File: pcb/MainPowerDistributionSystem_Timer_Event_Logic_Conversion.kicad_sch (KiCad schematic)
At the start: 4 parts

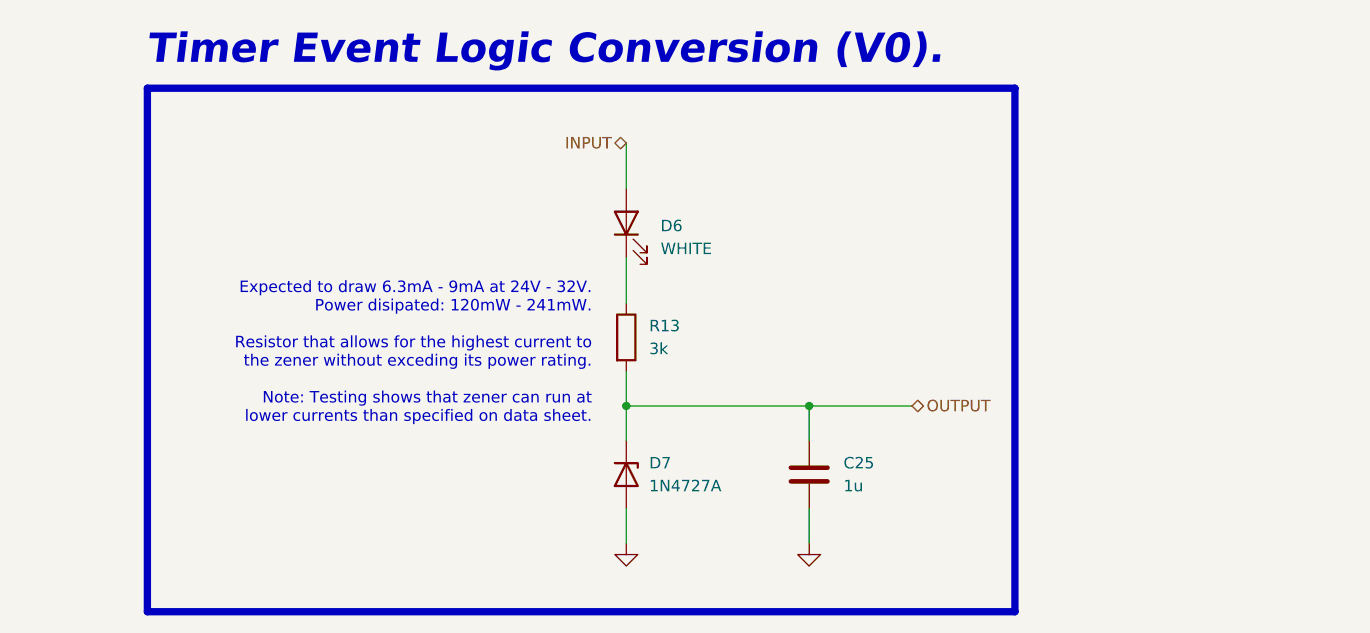
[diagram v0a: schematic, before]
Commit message: Fixed issues reported by `checkPCBs` concerning the stack connectors.
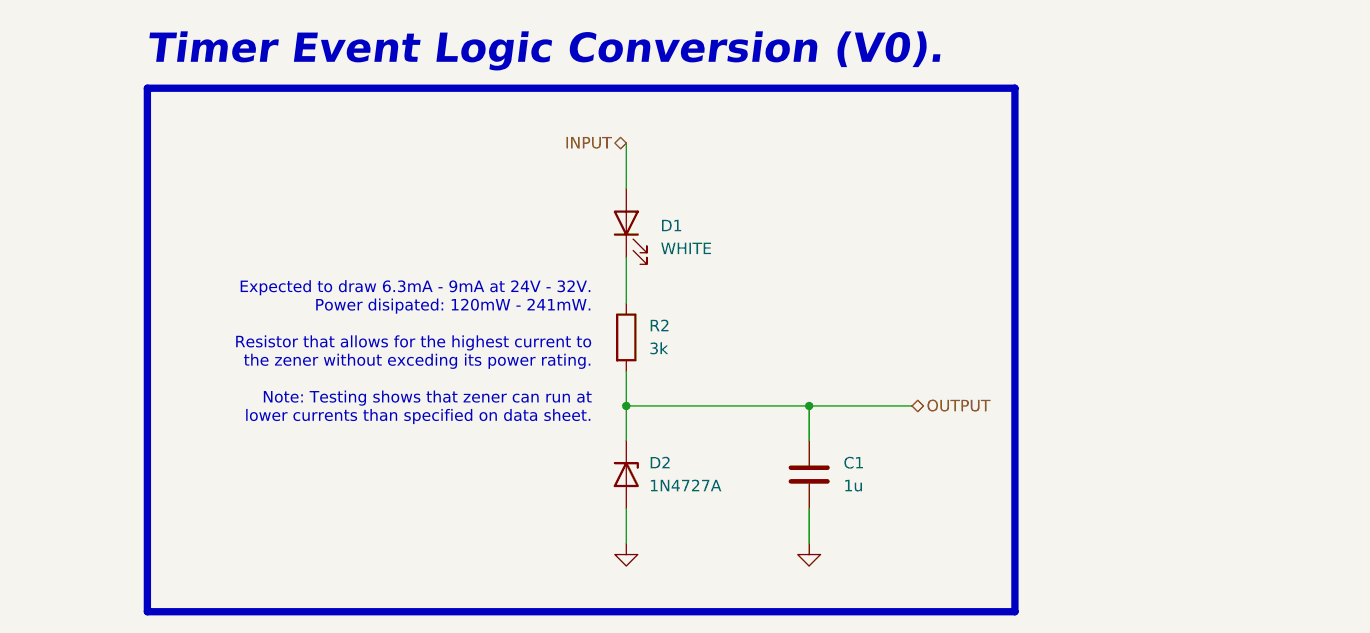
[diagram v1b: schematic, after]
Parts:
- renumbered C25 to C1, D6 to D1, D7 to D2, R13 to R2
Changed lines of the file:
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@@
 		(dnp no)
 		(fields_autoplaced yes)
-		(property "Reference" "C25"
+		(property "Reference" "C1"
 			(at 138.43 91.4399 0)
 			(effects
@@
 				(path "/92a7a41c-8494-4e4b-ac2d-deb1f1cd8085/54620fe3-2093-4758-a776-838cd07d45c6"
 					(reference "C25")
+					(unit 1)
+				)
+			)
+			(project "MainPowerDistributionSystem"
+				(path "/f4672588-55b2-48e9-8f23-132a69134eb2/261c9762-dbc6-4b8c-91f7-76f368e53a64"
+					(reference "C1")
+					(unit 1)
+				)
+				(path "/f4672588-55b2-48e9-8f23-132a69134eb2/3f92f74e-3cca-4282-aab2-357fe1c1118f"
+					(reference "C3")
+					(unit 1)
+				)
+				(path "/f4672588-55b2-48e9-8f23-132a69134eb2/41b9944a-f63d-4ce0-843f-6c1f8b109fe2"
+					(reference "C20")
+					(unit 1)
+				)
+				(path "/f4672588-55b2-48e9-8f23-132a69134eb2/5794667a-7b17-4495-a615-6983a1fee026"
+					(reference "C2")
+					(unit 1)
+				)
+				(path "/f4672588-55b2-48e9-8f23-132a69134eb2/5cd708ab-f243-4c3d-b9a6-6ef81c5046b4"
+					(reference "C21")
+					(unit 1)
+				)
+				(path "/f4672588-55b2-48e9-8f23-132a69134eb2/7bfeb19b-cfbf-4688-9fe2-f6b9e19ab4b8"
+					(reference "C19")
+					(unit 1)
+				)
+				(path "/f4672588-55b2-48e9-8f23-132a69134eb2/808cc913-2635-4e01-9a87-a42fd91b330a"
+					(reference "C18")
 					(unit 1)
 				)
@@
 		(dnp no)
 		(fields_autoplaced yes)
-		(property "Reference" "#PWR014"
+		(property "Reference" "#PWR056"
 			(at 114.3 106.68 0)
 			(effects
@@
 				(path "/92a7a41c-8494-4e4b-ac2d-deb1f1cd8085/54620fe3-2093-4758-a776-838cd07d45c6"
 					(reference "#PWR014")
+					(unit 1)
+				)
+			)
+			(project "MainPowerDistributionSystem"
+				(path "/f4672588-55b2-48e9-8f23-132a69134eb2/261c9762-dbc6-4b8c-91f7-76f368e53a64"
+					(reference "#PWR056")
+					(unit 1)
+				)
+				(path "/f4672588-55b2-48e9-8f23-132a69134eb2/3f92f74e-3cca-4282-aab2-357fe1c1118f"
+					(reference "#PWR060")
+					(unit 1)
+				)
+				(path "/f4672588-55b2-48e9-8f23-132a69134eb2/41b9944a-f63d-4ce0-843f-6c1f8b109fe2"
+					(reference "#PWR078")
+					(unit 1)
+				)
+				(path "/f4672588-55b2-48e9-8f23-132a69134eb2/5794667a-7b17-4495-a615-6983a1fee026"
+					(reference "#PWR058")
+					(unit 1)
+				)
+				(path "/f4672588-55b2-48e9-8f23-132a69134eb2/5cd708ab-f243-4c3d-b9a6-6ef81c5046b4"
+					(reference "#PWR080")
+					(unit 1)
+				)
+				(path "/f4672588-55b2-48e9-8f23-132a69134eb2/7bfeb19b-cfbf-4688-9fe2-f6b9e19ab4b8"
+					(reference "#PWR076")
+					(unit 1)
+				)
+				(path "/f4672588-55b2-48e9-8f23-132a69134eb2/808cc913-2635-4e01-9a87-a42fd91b330a"
+					(reference "#PWR074")
 					(unit 1)
 				)
@@
 		(dnp no)
 		(fields_autoplaced yes)
-		(property "Reference" "D6"
+		(property "Reference" "D1"
 			(at 118.11 65.0874 90)
 			(effects
@@
 				(path "/92a7a41c-8494-4e4b-ac2d-deb1f1cd8085/54620fe3-2093-4758-a776-838cd07d45c6"
 					(reference "D6")
+					(unit 1)
+				)
+			)
+			(project "MainPowerDistributionSystem"
+				(path "/f4672588-55b2-48e9-8f23-132a69134eb2/261c9762-dbc6-4b8c-91f7-76f368e53a64"
+					(reference "D1")
+					(unit 1)
+				)
+				(path "/f4672588-55b2-48e9-8f23-132a69134eb2/3f92f74e-3cca-4282-aab2-357fe1c1118f"
+					(reference "D5")
+					(unit 1)
+				)
+				(path "/f4672588-55b2-48e9-8f23-132a69134eb2/41b9944a-f63d-4ce0-843f-6c1f8b109fe2"
+					(reference "D11")
+					(unit 1)
+				)
+				(path "/f4672588-55b2-48e9-8f23-132a69134eb2/5794667a-7b17-4495-a615-6983a1fee026"
+					(reference "D3")
+					(unit 1)
+				)
+				(path "/f4672588-55b2-48e9-8f23-132a69134eb2/5cd708ab-f243-4c3d-b9a6-6ef81c5046b4"
+					(reference "D13")
+					(unit 1)
+				)
+				(path "/f4672588-55b2-48e9-8f23-132a69134eb2/7bfeb19b-cfbf-4688-9fe2-f6b9e19ab4b8"
+					(reference "D9")
+					(unit 1)
+				)
+				(path "/f4672588-55b2-48e9-8f23-132a69134eb2/808cc913-2635-4e01-9a87-a42fd91b330a"
+					(reference "D7")
 					(unit 1)
 				)
@@
 		(dnp no)
 		(fields_autoplaced yes)
-		(property "Reference" "R13"
+		(property "Reference" "R2"
 			(at 116.84 76.1999 0)
 			(effects
@@
 			(project "VehiclePowerDistributionSystem"
 				(path "/92a7a41c-8494-4e4b-ac2d-deb1f1cd8085/54620fe3-2093-4758-a776-838cd07d45c6"
+					(reference "R13")
+					(unit 1)
+				)
+			)
+			(project "MainPowerDistributionSystem"
+				(path "/f4672588-55b2-48e9-8f23-132a69134eb2/261c9762-dbc6-4b8c-91f7-76f368e53a64"
+					(reference "R2")
+					(unit 1)
+				)
+				(path "/f4672588-55b2-48e9-8f23-132a69134eb2/3f92f74e-3cca-4282-aab2-357fe1c1118f"
+					(reference "R4")
+					(unit 1)
+				)
+				(path "/f4672588-55b2-48e9-8f23-132a69134eb2/41b9944a-f63d-4ce0-843f-6c1f8b109fe2"
+					(reference "R15")
+					(unit 1)
+				)
+				(path "/f4672588-55b2-48e9-8f23-132a69134eb2/5794667a-7b17-4495-a615-6983a1fee026"
+					(reference "R3")
+					(unit 1)
+				)
+				(path "/f4672588-55b2-48e9-8f23-132a69134eb2/5cd708ab-f243-4c3d-b9a6-6ef81c5046b4"
+					(reference "R16")
+					(unit 1)
+				)
+				(path "/f4672588-55b2-48e9-8f23-132a69134eb2/7bfeb19b-cfbf-4688-9fe2-f6b9e19ab4b8"
+					(reference "R14")
+					(unit 1)
+				)
+				(path "/f4672588-55b2-48e9-8f23-132a69134eb2/808cc913-2635-4e01-9a87-a42fd91b330a"
 					(reference "R13")
 					(unit 1)
@@
 		(dnp no)
 		(fields_autoplaced yes)
-		(property "Reference" "#PWR015"
+		(property "Reference" "#PWR057"
 			(at 134.62 106.68 0)
 			(effects
@@
 				(path "/92a7a41c-8494-4e4b-ac2d-deb1f1cd8085/54620fe3-2093-4758-a776-838cd07d45c6"
 					(reference "#PWR015")
+					(unit 1)
+				)
+			)
+			(project "MainPowerDistributionSystem"
+				(path "/f4672588-55b2-48e9-8f23-132a69134eb2/261c9762-dbc6-4b8c-91f7-76f368e53a64"
+					(reference "#PWR057")
+					(unit 1)
+				)
+				(path "/f4672588-55b2-48e9-8f23-132a69134eb2/3f92f74e-3cca-4282-aab2-357fe1c1118f"
+					(reference "#PWR061")
+					(unit 1)
+				)
+				(path "/f4672588-55b2-48e9-8f23-132a69134eb2/41b9944a-f63d-4ce0-843f-6c1f8b109fe2"
+					(reference "#PWR079")
+					(unit 1)
+				)
+				(path "/f4672588-55b2-48e9-8f23-132a69134eb2/5794667a-7b17-4495-a615-6983a1fee026"
+					(reference "#PWR059")
+					(unit 1)
+				)
+				(path "/f4672588-55b2-48e9-8f23-132a69134eb2/5cd708ab-f243-4c3d-b9a6-6ef81c5046b4"
+					(reference "#PWR081")
+					(unit 1)
+				)
+				(path "/f4672588-55b2-48e9-8f23-132a69134eb2/7bfeb19b-cfbf-4688-9fe2-f6b9e19ab4b8"
+					(reference "#PWR077")
+					(unit 1)
+				)
+				(path "/f4672588-55b2-48e9-8f23-132a69134eb2/808cc913-2635-4e01-9a87-a42fd91b330a"
+					(reference "#PWR075")
 					(unit 1)
 				)
@@
 		(dnp no)
 		(fields_autoplaced yes)
-		(property "Reference" "D7"
+		(property "Reference" "D2"
 			(at 116.84 91.4399 90)
 			(effects
@@
 					(unit 1)
 				)
+			)
+			(project "MainPowerDistributionSystem"
+				(path "/f4672588-55b2-48e9-8f23-132a69134eb2/261c9762-dbc6-4b8c-91f7-76f368e53a64"
+					(reference "D2")
+					(unit 1)
+				)
+				(path "/f4672588-55b2-48e9-8f23-132a69134eb2/3f92f74e-3cca-4282-aab2-357fe1c1118f"
+					(reference "D6")
+					(unit 1)
+				)
+				(path "/f4672588-55b2-48e9-8f23-132a69134eb2/41b9944a-f63d-4ce0-843f-6c1f8b109fe2"
+					(reference "D12")
+					(unit 1)
+				)
+				(path "/f4672588-55b2-48e9-8f23-132a69134eb2/5794667a-7b17-4495-a615-6983a1fee026"
+					(reference "D4")
+					(unit 1)
+				)
+				(path "/f4672588-55b2-48e9-8f23-132a69134eb2/5cd708ab-f243-4c3d-b9a6-6ef81c5046b4"
+					(reference "D14")
+					(unit 1)
+				)
+				(path "/f4672588-55b2-48e9-8f23-132a69134eb2/7bfeb19b-cfbf-4688-9fe2-f6b9e19ab4b8"
+					(reference "D10")
+					(unit 1)
+				)
+				(path "/f4672588-55b2-48e9-8f23-132a69134eb2/808cc913-2635-4e01-9a87-a42fd91b330a"
+					(reference "D8")
+					(unit 1)
+				)

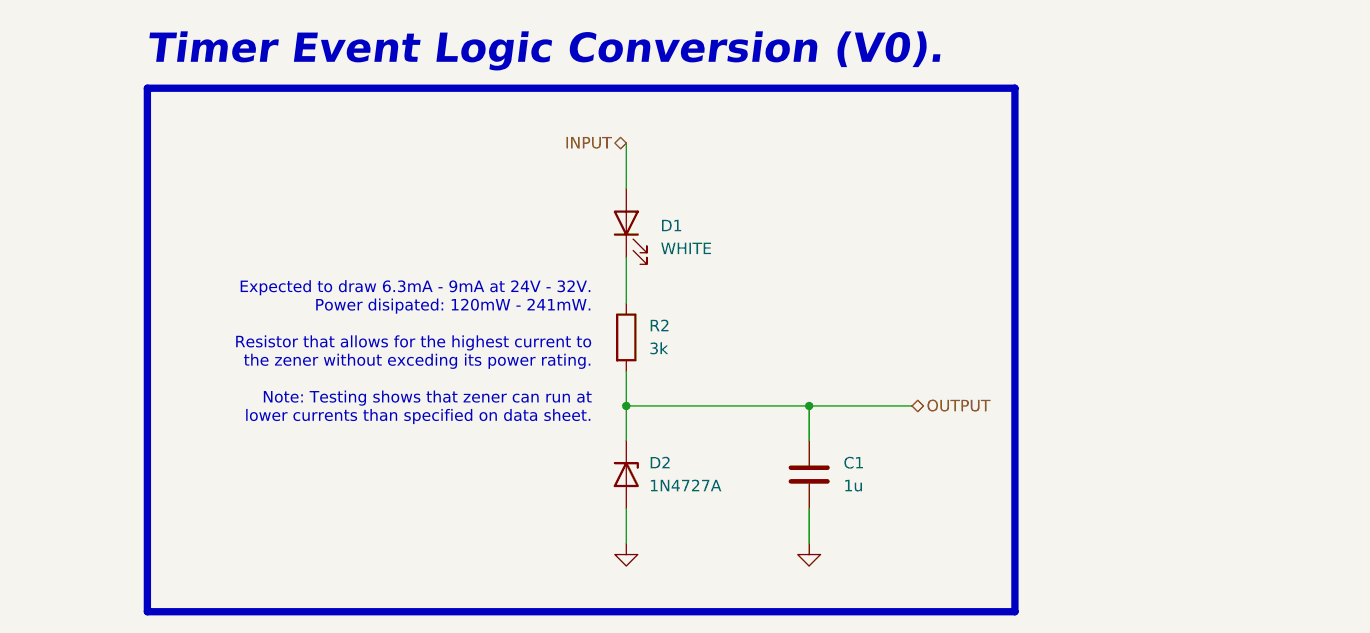
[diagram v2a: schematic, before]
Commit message: Mostly finalized `MainPowerDistributionSystem`.
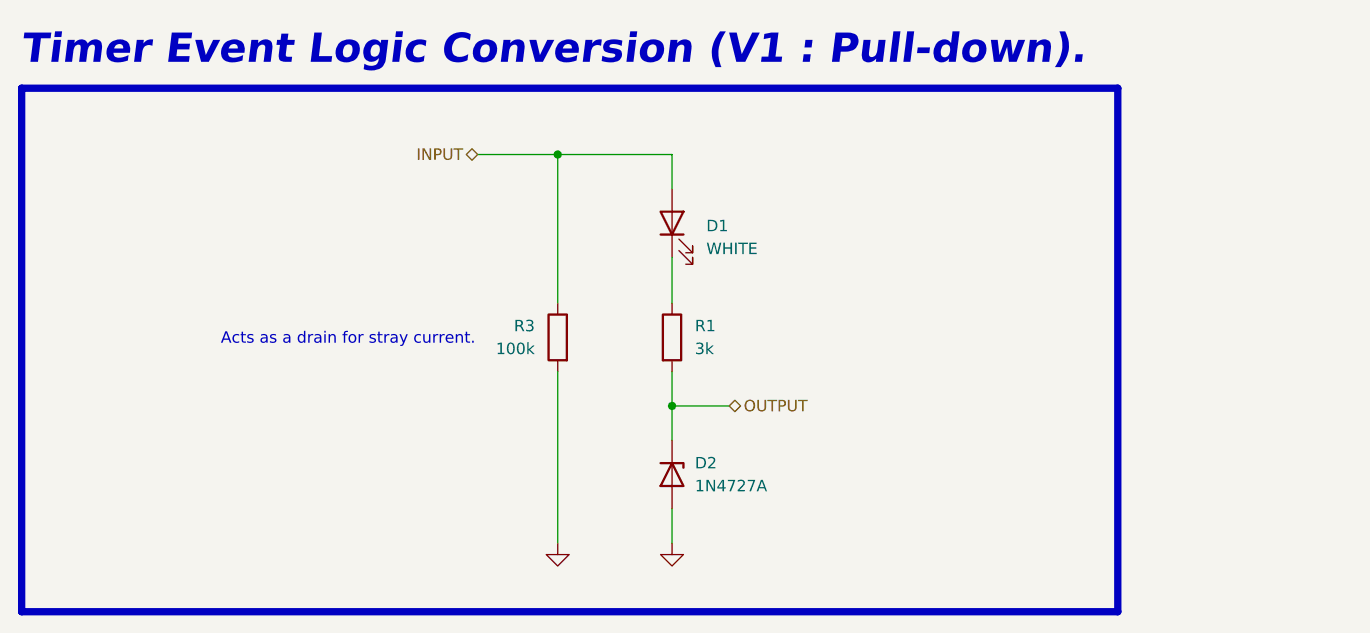
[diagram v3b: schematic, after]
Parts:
- removed C1: 1u, Capacitor_SMD:C_1206_3216Metric_Pad1.33x1.80mm_HandSolder, symbol Device:C
- added R3: 100k, Resistor_SMD:R_1206_3216Metric_Pad1.30x1.75mm_HandSolder, symbol Device:R
- renumbered R2 to R1
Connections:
- net GND: now also R3.2
- net INPUT: now also R3.1
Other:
- note added: "Acts as a drain for stray current."
- note added: "Timer Event Logic Conversion (V1 : Pull-down)."
- note removed: "Expected to draw 6.3mA - 9mA at 24V - 32V. Power disipated: 120mW - 241mW. Resistor that allows for the highest current to the zener without exceding its power rating. Note: Testing shows that zener can run at lower currents than specified on data sheet."
- note removed: "Timer Event Logic Conversion (V0)."
- moved on the sheet: D1, D2, R1
